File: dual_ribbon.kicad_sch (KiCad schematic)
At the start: 54 parts, among them J1 Conn_01x02_Socket, J2 Conn_01x02_Socket, J3 Conn_01x02_Socket, J4 Conn_01x02_Socket, Q1 PNP, Q2 MMBF4391, Q3 MMBF4391, U1 LM4041LP-ADJ, U2 TL072, U3 OPA2134, U4 TL072, U5 TL072

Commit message: Change parts to THT and do a test layout and route
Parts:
- C3, C4: footprint Capacitor_SMD:C_0805_2012Metric -> Capacitor_THT:C_Rect_L7.2mm_W2.5mm_P5.00mm_FKS2_FKP2_MKS2_MKP2
- D2, D3: footprint Diode_SMD:D_0805_2012Metric -> Diode_THT:D_DO-35_SOD27_P7.62mm_Horizontal
- Q1, Q2, Q3: footprint Package_TO_SOT_SMD:SOT-23 -> Package_TO_SOT_THT:TO-92_Inline
- R1, R10, R11, R12, R13, R14, R15, R16, R17, R18, R19, R2, R20, R21, R22, R23, R24, R3, R4, R5, R6, R7, R8, R9: footprint Resistor_SMD:R_0805_2012Metric -> Resistor_THT:R_Axial_DIN0207_L6.3mm_D2.5mm_P7.62mm_Horizontal
- U2, U3, U4, U5: footprint Package_SO:SOIC-8_3.9x4.9mm_P1.27mm -> Package_DIP:DIP-8_W7.62mm_Socket
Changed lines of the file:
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@@
 			)
 		)
-		(property "Footprint" "Package_TO_SOT_SMD:SOT-23"
+		(property "Footprint" "Package_TO_SOT_THT:TO-92_Inline"
 			(at 130.175 66.04 0)
 			(effects
@@
 			)
 		)
-		(property "Footprint" "Resistor_SMD:R_0805_2012Metric"
+		(property "Footprint" "Resistor_THT:R_Axial_DIN0207_L6.3mm_D2.5mm_P7.62mm_Horizontal"
 			(at 67.056 115.824 90)
 			(effects
@@
 			)
 		)
-		(property "Footprint" "Package_SO:SOIC-8_3.9x4.9mm_P1.27mm"
+		(property "Footprint" "Package_DIP:DIP-8_W7.62mm_Socket"
 			(at 96.52 132.08 0)
 			(effects
@@
 			)
 		)
-		(property "Footprint" "Resistor_SMD:R_0805_2012Metric"
+		(property "Footprint" "Resistor_THT:R_Axial_DIN0207_L6.3mm_D2.5mm_P7.62mm_Horizontal"
 			(at 148.844 98.044 90)
 			(effects
@@
 			)
 		)
-		(property "Footprint" "Resistor_SMD:R_0805_2012Metric"
+		(property "Footprint" "Resistor_THT:R_Axial_DIN0207_L6.3mm_D2.5mm_P7.62mm_Horizontal"
 			(at 203.454 66.294 90)
 			(effects
@@
 			)
 		)
-		(property "Footprint" "Capacitor_SMD:C_0805_2012Metric"
+		(property "Footprint" "Capacitor_THT:C_Rect_L7.2mm_W2.5mm_P5.00mm_FKS2_FKP2_MKS2_MKP2"
 			(at 106.68 106.3752 0)
 			(effects
@@
 			)
 		)
-		(property "Footprint" "Resistor_SMD:R_0805_2012Metric"
+		(property "Footprint" "Resistor_THT:R_Axial_DIN0207_L6.3mm_D2.5mm_P7.62mm_Horizontal"
 			(at 203.454 86.614 90)
 			(effects
@@
 			)
 		)
-		(property "Footprint" "Package_SO:SOIC-8_3.9x4.9mm_P1.27mm"
+		(property "Footprint" "Package_DIP:DIP-8_W7.62mm_Socket"
 			(at 149.86 91.44 0)
 			(effects
@@
 			)
 		)
-		(property "Footprint" "Resistor_SMD:R_0805_2012Metric"
+		(property "Footprint" "Resistor_THT:R_Axial_DIN0207_L6.3mm_D2.5mm_P7.62mm_Horizontal"
 			(at 148.844 77.724 90)
 			(effects
@@
 			)
 		)
-		(property "Footprint" "Resistor_SMD:R_0805_2012Metric"
+		(property "Footprint" "Resistor_THT:R_Axial_DIN0207_L6.3mm_D2.5mm_P7.62mm_Horizontal"
 			(at 118.364 112.014 90)
 			(effects
@@
 			)
 		)
-		(property "Footprint" "Package_SO:SOIC-8_3.9x4.9mm_P1.27mm"
+		(property "Footprint" "Package_DIP:DIP-8_W7.62mm_Socket"
 			(at 54.61 158.75 0)
 			(effects
@@
 			)
 		)
-		(property "Footprint" "Resistor_SMD:R_0805_2012Metric"
+		(property "Footprint" "Resistor_THT:R_Axial_DIN0207_L6.3mm_D2.5mm_P7.62mm_Horizontal"
 			(at 101.854 106.934 90)
 			(effects
@@
 			)
 		)
-		(property "Footprint" "Resistor_SMD:R_0805_2012Metric"
+		(property "Footprint" "Resistor_THT:R_Axial_DIN0207_L6.3mm_D2.5mm_P7.62mm_Horizontal"
 			(at 129.794 122.936 90)
 			(effects
@@
 			)
 		)
-		(property "Footprint" "Package_SO:SOIC-8_3.9x4.9mm_P1.27mm"
+		(property "Footprint" "Package_DIP:DIP-8_W7.62mm_Socket"
 			(at 149.86 71.12 0)
 			(effects
@@
 			)
 		)
-		(property "Footprint" "Resistor_SMD:R_0805_2012Metric"
+		(property "Footprint" "Resistor_THT:R_Axial_DIN0207_L6.3mm_D2.5mm_P7.62mm_Horizontal"
 			(at 122.174 122.936 90)
 			(effects
@@
 			)
 		)
-		(property "Footprint" "Resistor_SMD:R_0805_2012Metric"
+		(property "Footprint" "Resistor_THT:R_Axial_DIN0207_L6.3mm_D2.5mm_P7.62mm_Horizontal"
 			(at 192.024 76.454 90)
 			(effects
@@
 			)
 		)
-		(property "Footprint" "Package_SO:SOIC-8_3.9x4.9mm_P1.27mm"
+		(property "Footprint" "Package_DIP:DIP-8_W7.62mm_Socket"
 			(at 111.76 88.9 0)
 			(effects
@@
 			)
 		)
-		(property "Footprint" "Package_SO:SOIC-8_3.9x4.9mm_P1.27mm"
+		(property "Footprint" "Package_DIP:DIP-8_W7.62mm_Socket"
 			(at 36.83 158.75 0)
 			(effects
@@
 			)
 		)
-		(property "Footprint" "Resistor_SMD:R_0805_2012Metric"
+		(property "Footprint" "Resistor_THT:R_Axial_DIN0207_L6.3mm_D2.5mm_P7.62mm_Horizontal"
 			(at 65.024 103.886 90)
 			(effects
@@
 			)
 		)
-		(property "Footprint" "Package_TO_SOT_SMD:SOT-23"
+		(property "Footprint" "Package_TO_SOT_THT:TO-92_Inline"
 			(at 90.17 59.69 0)
 			(effects
@@
 			)
 		)
-		(property "Footprint" "Diode_SMD:D_0805_2012Metric"
+		(property "Footprint" "Diode_THT:D_DO-35_SOD27_P7.62mm_Horizontal"
 			(at 92.71 107.95 0)
 			(effects
@@
 			)
 		)
-		(property "Footprint" "Resistor_SMD:R_0805_2012Metric"
+		(property "Footprint" "Resistor_THT:R_Axial_DIN0207_L6.3mm_D2.5mm_P7.62mm_Horizontal"
 			(at 141.986 82.804 90)
 			(effects
@@
 			)
 		)
-		(property "Footprint" "Resistor_SMD:R_0805_2012Metric"
+		(property "Footprint" "Resistor_THT:R_Axial_DIN0207_L6.3mm_D2.5mm_P7.62mm_Horizontal"
 			(at 58.166 25.654 90)
 			(effects
@@
 			)
 		)
-		(property "Footprint" "Package_SO:SOIC-8_3.9x4.9mm_P1.27mm"
+		(property "Footprint" "Package_DIP:DIP-8_W7.62mm_Socket"
 			(at 81.28 113.03 0)
 			(effects
@@
 			)
 		)
-		(property "Footprint" "Resistor_SMD:R_0805_2012Metric"
+		(property "Footprint" "Resistor_THT:R_Axial_DIN0207_L6.3mm_D2.5mm_P7.62mm_Horizontal"
 			(at 118.364 117.856 90)
 			(effects
@@
 			)
 		)
-		(property "Footprint" "Resistor_SMD:R_0805_2012Metric"
+		(property "Footprint" "Resistor_THT:R_Axial_DIN0207_L6.3mm_D2.5mm_P7.62mm_Horizontal"
 			(at 95.504 90.424 90)
 			(effects
@@
 			)
 		)
-		(property "Footprint" "Resistor_SMD:R_0805_2012Metric"
+		(property "Footprint" "Resistor_THT:R_Axial_DIN0207_L6.3mm_D2.5mm_P7.62mm_Horizontal"
 			(at 110.744 95.504 90)
 			(effects
@@
 			)
 		)
-		(property "Footprint" "Package_TO_SOT_SMD:SOT-23"
+		(property "Footprint" "Package_TO_SOT_THT:TO-92_Inline"
 			(at 130.175 86.36 0)
 			(effects
@@
 			)
 		)
-		(property "Footprint" "Resistor_SMD:R_0805_2012Metric"
+		(property "Footprint" "Resistor_THT:R_Axial_DIN0207_L6.3mm_D2.5mm_P7.62mm_Horizontal"
 			(at 141.986 103.124 90)
 			(effects
@@
 			)
 		)
-		(property "Footprint" "Resistor_SMD:R_0805_2012Metric"
+		(property "Footprint" "Resistor_THT:R_Axial_DIN0207_L6.3mm_D2.5mm_P7.62mm_Horizontal"
 			(at 95.504 70.104 90)
 			(effects
@@
 			)
 		)
-		(property "Footprint" "Package_SO:SOIC-8_3.9x4.9mm_P1.27mm"
+		(property "Footprint" "Package_DIP:DIP-8_W7.62mm_Socket"
 			(at 111.76 68.58 0)
 			(effects
@@
 			)
 		)
-		(property "Footprint" "Diode_SMD:D_0805_2012Metric"
+		(property "Footprint" "Diode_THT:D_DO-35_SOD27_P7.62mm_Horizontal"
 			(at 110.49 132.08 0)
 			(effects
@@
 			)
 		)
-		(property "Footprint" "Resistor_SMD:R_0805_2012Metric"
+		(property "Footprint" "Resistor_THT:R_Axial_DIN0207_L6.3mm_D2.5mm_P7.62mm_Horizontal"
 			(at 176.784 95.504 90)
 			(effects
@@
 			)
 		)
-		(property "Footprint" "Resistor_SMD:R_0805_2012Metric"
+		(property "Footprint" "Resistor_THT:R_Axial_DIN0207_L6.3mm_D2.5mm_P7.62mm_Horizontal"
 			(at 110.744 61.976 90)
 			(effects
@@
 			)
 		)
-		(property "Footprint" "Resistor_SMD:R_0805_2012Metric"
+		(property "Footprint" "Resistor_THT:R_Axial_DIN0207_L6.3mm_D2.5mm_P7.62mm_Horizontal"
 			(at 192.024 81.534 90)
 			(effects
@@
 			)
 		)
-		(property "Footprint" "Resistor_SMD:R_0805_2012Metric"
+		(property "Footprint" "Resistor_THT:R_Axial_DIN0207_L6.3mm_D2.5mm_P7.62mm_Horizontal"
 			(at 36.576 66.294 90)
 			(effects
@@
 			)
 		)
-		(property "Footprint" "Resistor_SMD:R_0805_2012Metric"
+		(property "Footprint" "Resistor_THT:R_Axial_DIN0207_L6.3mm_D2.5mm_P7.62mm_Horizontal"
 			(at 106.426 137.414 90)
 			(effects
@@
 			)
 		)
-		(property "Footprint" "Package_SO:SOIC-8_3.9x4.9mm_P1.27mm"
+		(property "Footprint" "Package_DIP:DIP-8_W7.62mm_Socket"
 			(at 177.8 88.9 0)
 			(effects
@@
 			)
 		)
-		(property "Footprint" "Package_SO:SOIC-8_3.9x4.9mm_P1.27mm"
+		(property "Footprint" "Package_DIP:DIP-8_W7.62mm_Socket"
 			(at 204.47 80.01 0)
 			(effects
@@
 			)
 		)
-		(property "Footprint" "Resistor_SMD:R_0805_2012Metric"
+		(property "Footprint" "Resistor_THT:R_Axial_DIN0207_L6.3mm_D2.5mm_P7.62mm_Horizontal"
 			(at 165.354 90.424 90)
 			(effects
@@
 			)
 		)
-		(property "Footprint" "Package_SO:SOIC-8_3.9x4.9mm_P1.27mm"
+		(property "Footprint" "Package_DIP:DIP-8_W7.62mm_Socket"
 			(at 50.8 158.75 0)
 			(effects
@@
 			)
 		)
-		(property "Footprint" "Capacitor_SMD:C_0805_2012Metric"
+		(property "Footprint" "Capacitor_THT:C_Rect_L7.2mm_W2.5mm_P5.00mm_FKS2_FKP2_MKS2_MKP2"
 			(at 114.3 51.1048 0)
 			(effects
@@
 			)
 		)
-		(property "Footprint" "Package_SO:SOIC-8_3.9x4.9mm_P1.27mm"
+		(property "Footprint" "Package_DIP:DIP-8_W7.62mm_Socket"
 			(at 44.45 158.75 0)
 			(effects

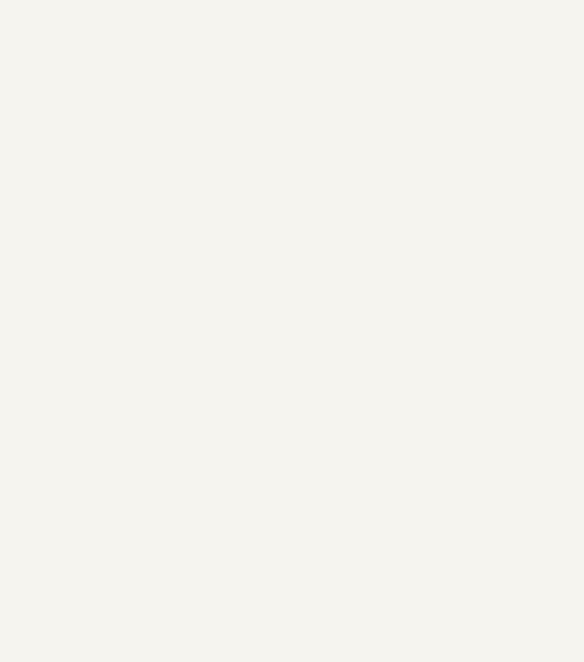
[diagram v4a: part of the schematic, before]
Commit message: Add delayed modulation to use up more board space
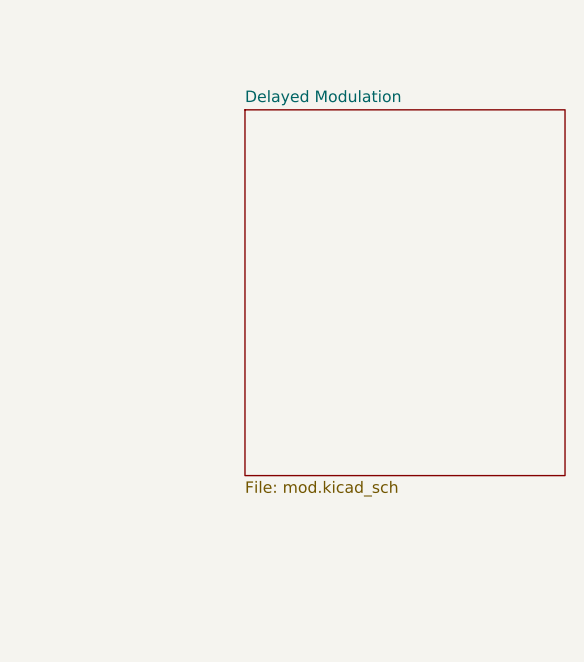
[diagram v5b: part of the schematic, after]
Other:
- added sheet Delayed Modulation (mod.kicad_sch)
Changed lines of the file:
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@@
+		)
+	)
+	(sheet
+		(at 412.75 22.86)
+		(size 35.56 40.64)
+		(fields_autoplaced yes)
+		(stroke
+			(width 0.1524)
+			(type solid)
+		)
+		(fill
+			(color 0 0 0 0.0000)
+		)
+		(property "Sheetname" "Delayed Modulation"
+			(at 412.75 22.1484 0)
+			(effects
+				(font
+					(size 1.27 1.27)
+				)
+				(justify left bottom)
+			)
+		)
+		(property "Sheetfile" "mod.kicad_sch"
+			(at 412.75 64.0846 0)
+			(effects
+				(font
+					(size 1.27 1.27)
+				)
+				(justify left top)
+			)
+		)
+		(instances
+			(project "dual_ribbon"
+				(path "/e71b1ffe-cd24-465b-817f-392629163705"
+					(page "2")
+				)
+			)
 		)
 	)

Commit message: Finish schematic for modulation
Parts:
- J1: value Conn_01x02_Socket -> HIGH OUT
- J2: value Conn_01x02_Socket -> DIFF OUT
- J3: value Conn_01x02_Socket -> LOW OUT
- J4: value Conn_01x02_Socket -> GATE OUT
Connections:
- net GATE: now reaches D3.2 (A), R24.1, U5.7
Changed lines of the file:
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@@
 	(wire
 		(pts
+			(xy 106.68 121.92) (xy 105.41 121.92)
+		)
+		(stroke
+			(width 0)
+			(type default)
+		)
+	)
+	(wire
+		(pts
 			(xy 195.58 77.47) (xy 196.85 77.47)
 		)
@@
 	(wire
 		(pts
+			(xy 105.41 121.92) (xy 105.41 132.08)
+		)
+		(stroke
+			(width 0)
+			(type default)
+		)
+	)
+	(wire
+		(pts
 			(xy 134.62 88.9) (xy 142.24 88.9)
 		)
@@
 		)
 	)
+	(global_label "GATE"
+		(shape input)
+		(at 106.68 121.92 0)
+		(fields_autoplaced yes)
+		(effects
+			(font
+				(size 1.27 1.27)
+			)
+			(justify left)
+		)
+		(property "Intersheetrefs" "${INTERSHEET_REFS}"
+			(at 114.1404 121.92 0)
+			(effects
+				(font
+					(size 1.27 1.27)
+				)
+				(justify left)
+				(hide yes)
+			)
+		)
+	)
 	(symbol
 		(lib_id "power:GND")
@@
 			)
 		)
-		(property "Value" "Conn_01x02_Socket"
+		(property "Value" "DIFF OUT"
 			(at 236.22 73.6599 0)
 			(effects
@@
 			)
 		)
-		(property "Value" "Conn_01x02_Socket"
+		(property "Value" "LOW OUT"
 			(at 199.39 102.8699 0)
 			(effects
@@
 			)
 		)
-		(property "Value" "Conn_01x02_Socket"
+		(property "Value" "HIGH OUT"
 			(at 181.61 64.7699 0)
 			(effects
@@
 			)
 		)
-		(property "Value" "Conn_01x02_Socket"
+		(property "Value" "GATE OUT"
 			(at 124.46 140.9699 0)
 			(effects
